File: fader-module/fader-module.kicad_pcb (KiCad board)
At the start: 2 copper layers, 75 x 100 mm, 40 parts, among them J1 Conn_1x05_Pin, J2 Conn_1x05_Socket, J3 Conn_01x02_Pin, J4 Conn_01x06_Pin, J6 Conn_01x06_Pin, SW1 1825910-6, SW2 1825910-6, U5 ATMEGA328P-AUR, U7 DRV8871DDAR

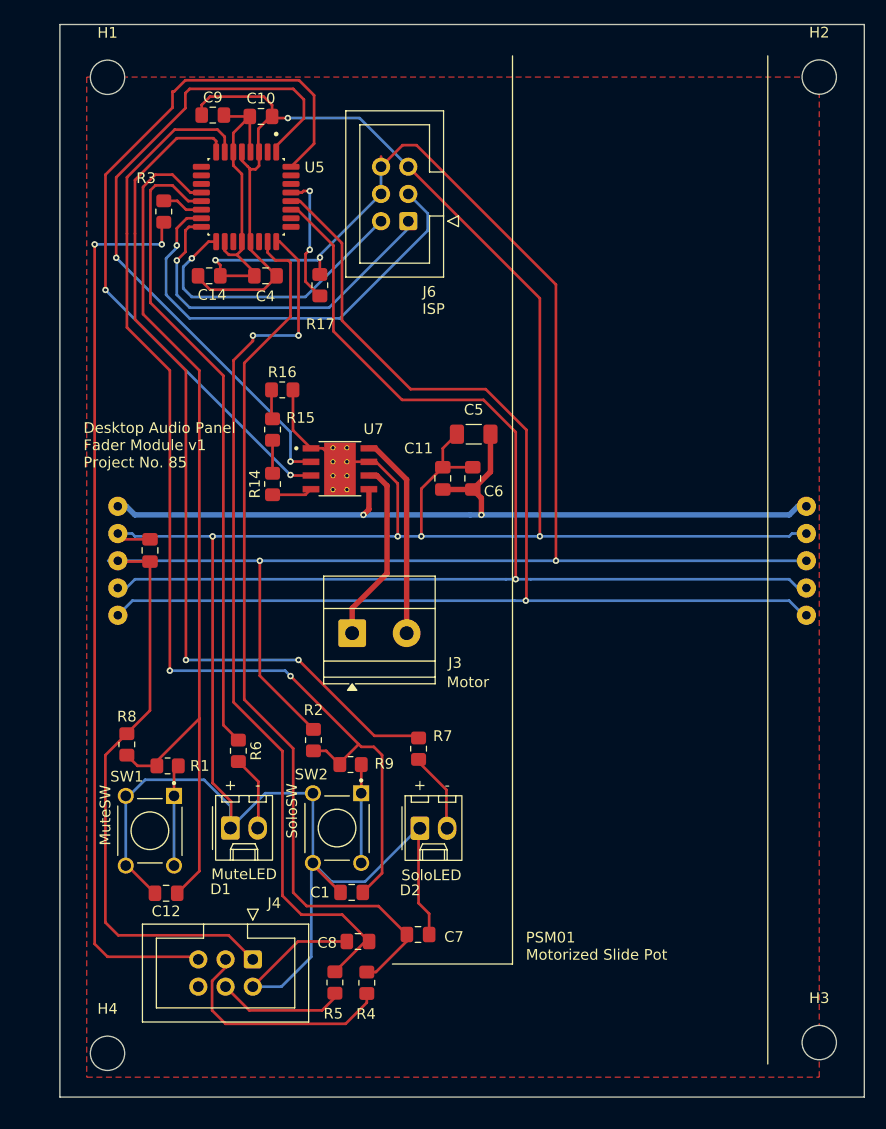
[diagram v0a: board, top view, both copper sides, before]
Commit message: aligned mounting holes
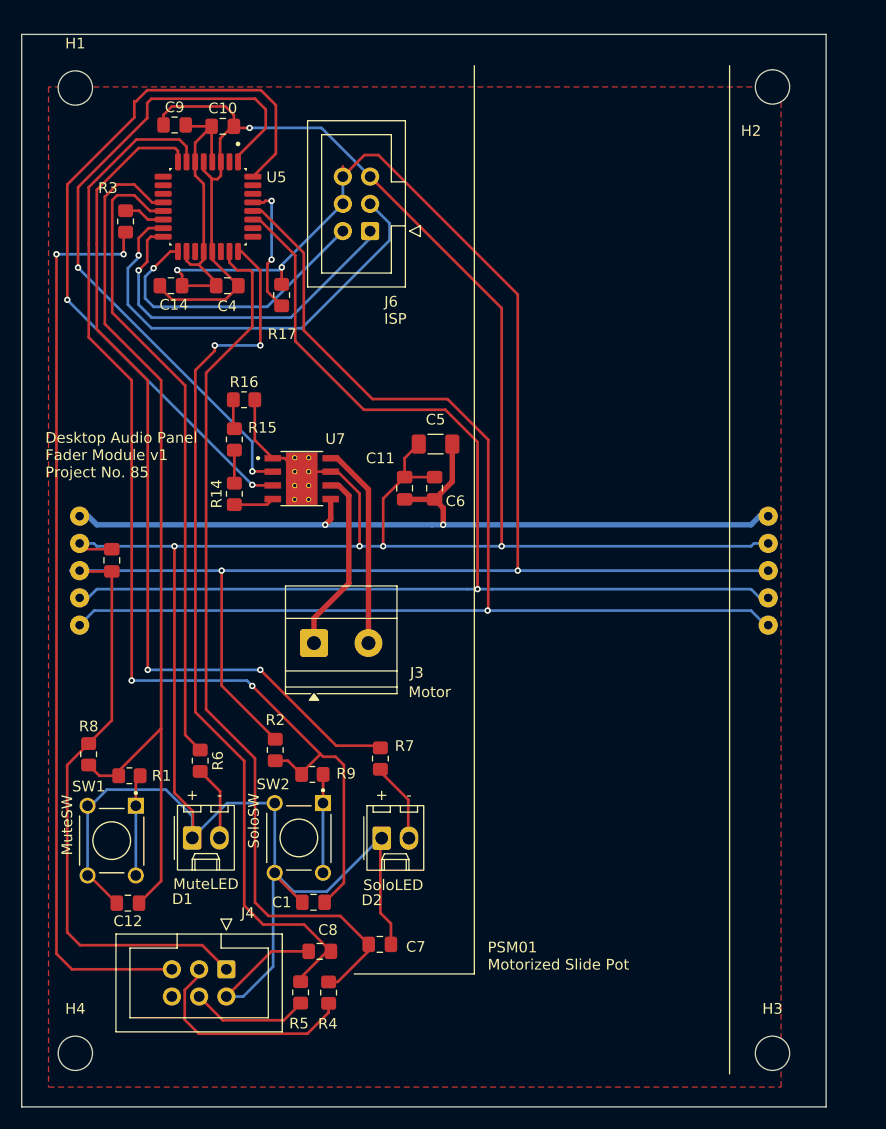
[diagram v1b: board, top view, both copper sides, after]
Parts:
- moved H3 4.47 mm to (195.0, 135.0)
- moved H2 4.46 mm to (195.0, 44.9)
- moved C1 3.68 mm to (152.2, 120.9)
- moved C12 3.68 mm to (134.9, 121.0)
- moved C5 3.68 mm to (163.6, 78.2)
- moved C7 3.68 mm to (158.4, 124.8)
- moved D1 3.68 mm to (140.9, 114.9)
- moved D2 3.68 mm to (158.6, 114.9)
- moved J1 3.68 mm to (130.4, 90.0)
- moved J2 3.68 mm to (194.6, 90.0)
- moved J3 3.68 mm to (152.2, 96.8)
- moved J6 3.68 mm to (157.5, 58.3)
- moved R2 3.68 mm to (148.6, 106.7)
- moved R6 3.68 mm to (141.6, 107.7)
- moved R7 3.68 mm to (158.4, 107.5)
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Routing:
- net GND: track 313.9 -> 311.7 mm
- net +3V3: track 237.4 -> 238.5 mm
- net /SERVO: track 12.0 -> 10.9 mm
- net /TOUCH: track 83.9 -> 85.0 mm
- net /LINE: track 21.9 -> 20.9 mm
